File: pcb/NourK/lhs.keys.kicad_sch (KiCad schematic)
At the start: 33 parts, among them SW10 OSKEY, SW11 GRAVE, SW12 A, SW13 S, SW14 D, SW15 F, SW16 G, SW17 LEFT_SHIFT, SW18 Z, SW19 X, SW20 C, SW21 V, SW22 B, SW23 LEFT_CTRL, SW24 LAYER1, SW25 LAYER2, SW26 LEFT_ALT, SW27 SPACE, SW3 ESCAPE, SW4 TAB, SW5 Q, SW6 W, SW7 E, SW8 R, SW9 T

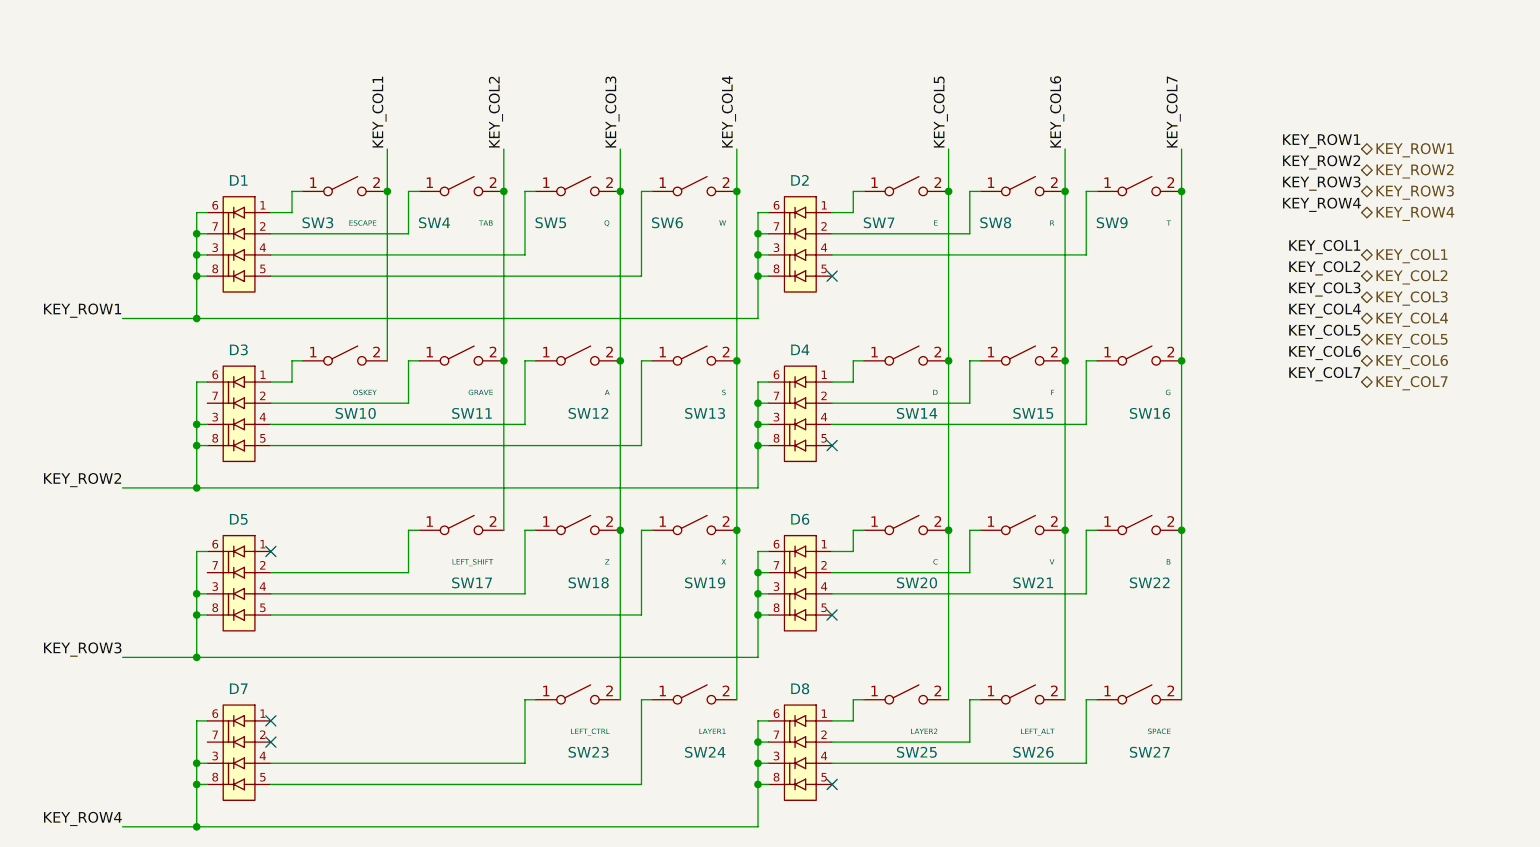
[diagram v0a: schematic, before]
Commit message: Add RHS schematics sheets
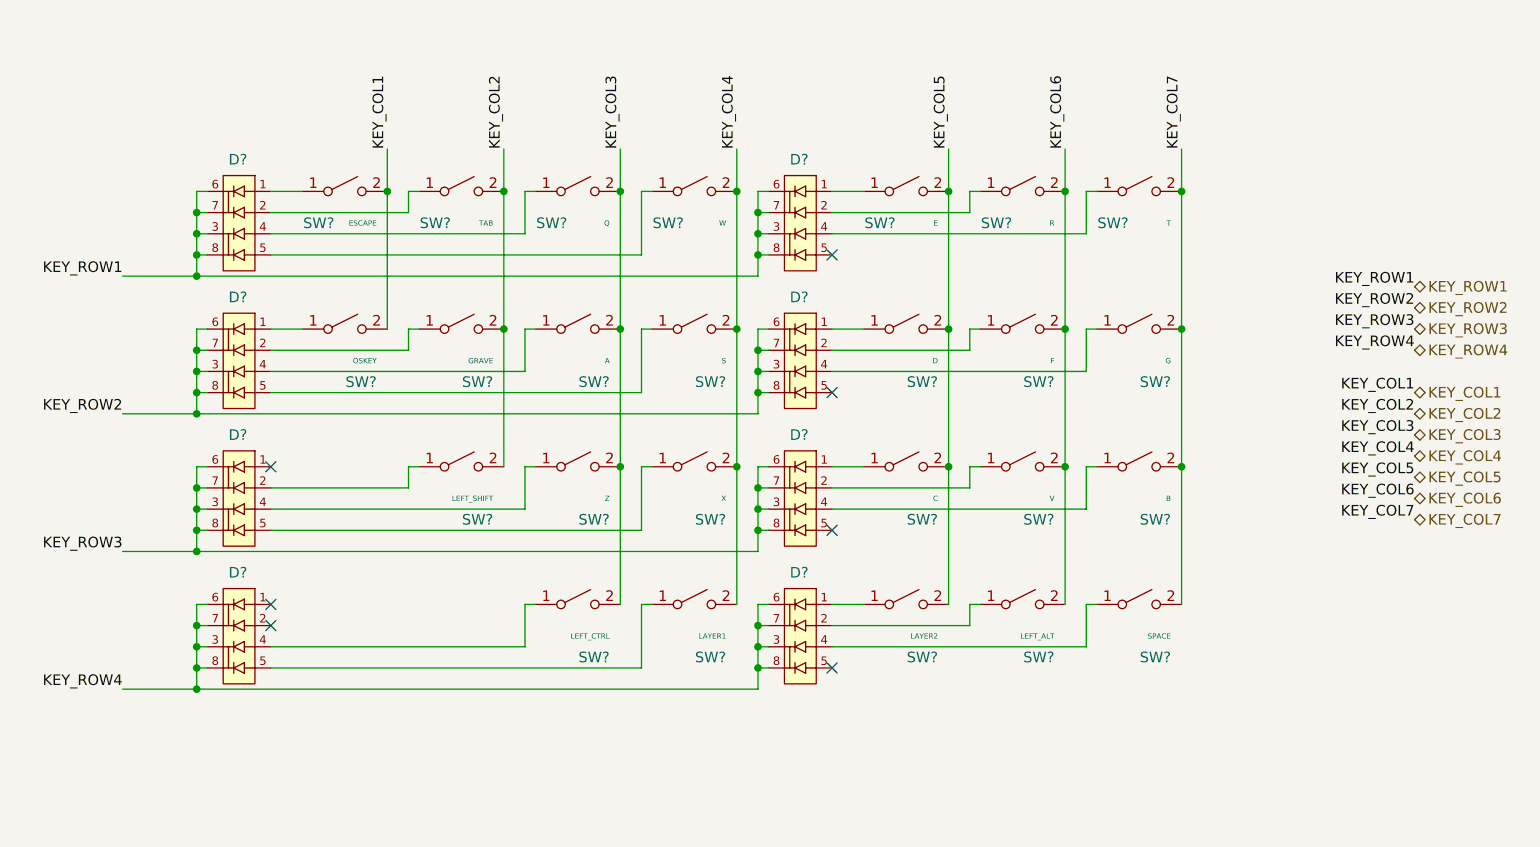
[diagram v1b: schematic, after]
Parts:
- removed D1, D2, D3, D4, D5, D6, D7, D8: BAV70SRAZ, Nour_KB:DIO_BAV70SRAZ, symbol Nour_KB:BAV70SRAZ
- removed SW10: OSKEY, Keebio-Parts:MX-Alps-Choc-1U-NoLED, symbol Switch:SW_SPST
- removed SW11: GRAVE, Keebio-Parts:MX-Alps-Choc-1U-NoLED, symbol Switch:SW_SPST
- removed SW12: A, Keebio-Parts:MX-Alps-Choc-1U-NoLED, symbol Switch:SW_SPST
- removed SW13: S, Keebio-Parts:MX-Alps-Choc-1U-NoLED, symbol Switch:SW_SPST
- removed SW14: D, Keebio-Parts:MX-Alps-Choc-1U-NoLED, symbol Switch:SW_SPST
- removed SW15: F, Keebio-Parts:MX-Alps-Choc-1U-NoLED, symbol Switch:SW_SPST
- removed SW16: G, Keebio-Parts:MX-Alps-Choc-1U-NoLED, symbol Switch:SW_SPST
- removed SW17: LEFT_SHIFT, Keebio-Parts:MX-Alps-Choc-1U-NoLED, symbol Switch:SW_SPST
- removed SW18: Z, Keebio-Parts:MX-Alps-Choc-1U-NoLED, symbol Switch:SW_SPST
- removed SW19: X, Keebio-Parts:MX-Alps-Choc-1U-NoLED, symbol Switch:SW_SPST
- removed SW20: C, Keebio-Parts:MX-Alps-Choc-1U-NoLED, symbol Switch:SW_SPST
- removed SW21: V, Keebio-Parts:MX-Alps-Choc-1U-NoLED, symbol Switch:SW_SPST
- removed SW22: B, Keebio-Parts:MX-Alps-Choc-1U-NoLED, symbol Switch:SW_SPST
- removed SW23: LEFT_CTRL, Keebio-Parts:MX-Alps-Choc-1U-NoLED, symbol Switch:SW_SPST
- removed SW24: LAYER1, Keebio-Parts:MX-Alps-Choc-1U-NoLED, symbol Switch:SW_SPST
- removed SW25: LAYER2, Keebio-Parts:MX-Alps-Choc-1U-NoLED, symbol Switch:SW_SPST
- removed SW26: LEFT_ALT, Keebio-Parts:MX-Alps-Choc-1U-NoLED, symbol Switch:SW_SPST
- removed SW27: SPACE, Keebio-Parts:MX-Alps-Choc-1U-NoLED, symbol Switch:SW_SPST
- removed SW3: ESCAPE, Keebio-Parts:MX-Alps-Choc-1U-NoLED, symbol Switch:SW_SPST
- removed SW4: TAB, Keebio-Parts:MX-Alps-Choc-1U-NoLED, symbol Switch:SW_SPST
- removed SW5: Q, Keebio-Parts:MX-Alps-Choc-1U-NoLED, symbol Switch:SW_SPST
- removed SW6: W, Keebio-Parts:MX-Alps-Choc-1U-NoLED, symbol Switch:SW_SPST
- removed SW7: E, Keebio-Parts:MX-Alps-Choc-1U-NoLED, symbol Switch:SW_SPST
- removed SW8: R, Keebio-Parts:MX-Alps-Choc-1U-NoLED, symbol Switch:SW_SPST
- removed SW9: T, Keebio-Parts:MX-Alps-Choc-1U-NoLED, symbol Switch:SW_SPST
- added D? (x8): BAV70SRAZ, Nour_KB:DIO_BAV70SRAZ, symbol Nour_KB:BAV70SRAZ
- added SW?: B, Keebio-Parts:MX-Alps-Choc-1U-NoLED, symbol Switch:SW_SPST
- added SW?: OSKEY, Keebio-Parts:MX-Alps-Choc-1U-NoLED, symbol Switch:SW_SPST
- added SW?: G, Keebio-Parts:MX-Alps-Choc-1U-NoLED, symbol Switch:SW_SPST
- added SW?: T, Keebio-Parts:MX-Alps-Choc-1U-NoLED, symbol Switch:SW_SPST
- added SW?: C, Keebio-Parts:MX-Alps-Choc-1U-NoLED, symbol Switch:SW_SPST
- added SW?: S, Keebio-Parts:MX-Alps-Choc-1U-NoLED, symbol Switch:SW_SPST
- added SW?: ESCAPE, Keebio-Parts:MX-Alps-Choc-1U-NoLED, symbol Switch:SW_SPST
- added SW?: Z, Keebio-Parts:MX-Alps-Choc-1U-NoLED, symbol Switch:SW_SPST
- added SW?: W, Keebio-Parts:MX-Alps-Choc-1U-NoLED, symbol Switch:SW_SPST
- added SW?: LAYER1, Keebio-Parts:MX-Alps-Choc-1U-NoLED, symbol Switch:SW_SPST
- added SW?: SPACE, Keebio-Parts:MX-Alps-Choc-1U-NoLED, symbol Switch:SW_SPST
- added SW?: R, Keebio-Parts:MX-Alps-Choc-1U-NoLED, symbol Switch:SW_SPST
- added SW?: LEFT_ALT, Keebio-Parts:MX-Alps-Choc-1U-NoLED, symbol Switch:SW_SPST
- added SW?: Q, Keebio-Parts:MX-Alps-Choc-1U-NoLED, symbol Switch:SW_SPST
- added SW?: V, Keebio-Parts:MX-Alps-Choc-1U-NoLED, symbol Switch:SW_SPST
- added SW?: TAB, Keebio-Parts:MX-Alps-Choc-1U-NoLED, symbol Switch:SW_SPST
- added SW?: LEFT_CTRL, Keebio-Parts:MX-Alps-Choc-1U-NoLED, symbol Switch:SW_SPST
- added SW?: D, Keebio-Parts:MX-Alps-Choc-1U-NoLED, symbol Switch:SW_SPST
- added SW?: F, Keebio-Parts:MX-Alps-Choc-1U-NoLED, symbol Switch:SW_SPST
- added SW?: GRAVE, Keebio-Parts:MX-Alps-Choc-1U-NoLED, symbol Switch:SW_SPST
- added SW?: LEFT_SHIFT, Keebio-Parts:MX-Alps-Choc-1U-NoLED, symbol Switch:SW_SPST
- added SW?: LAYER2, Keebio-Parts:MX-Alps-Choc-1U-NoLED, symbol Switch:SW_SPST
- added SW?: E, Keebio-Parts:MX-Alps-Choc-1U-NoLED, symbol Switch:SW_SPST
- added SW?: A, Keebio-Parts:MX-Alps-Choc-1U-NoLED, symbol Switch:SW_SPST
- added SW?: X, Keebio-Parts:MX-Alps-Choc-1U-NoLED, symbol Switch:SW_SPST
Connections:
- net KEY_COL1: now also SW?.2 (B), SW?.2 (B)
- net KEY_COL2: now also SW?.2 (B), SW?.2 (B), SW?.2 (B)
- net KEY_COL3: now also SW?.2 (B), SW?.2 (B), SW?.2 (B), SW?.2 (B)
- net KEY_COL4: now also SW?.2 (B), SW?.2 (B), SW?.2 (B), SW?.2 (B)
- net KEY_COL5: now also SW?.2 (B), SW?.2 (B), SW?.2 (B), SW?.2 (B)
- net KEY_COL6: now also SW?.2 (B), SW?.2 (B), SW?.2 (B), SW?.2 (B)
- net KEY_COL7: now also SW?.2 (B), SW?.2 (B), SW?.2 (B), SW?.2 (B)
- net KEY_ROW1: now also D?.3, D?.3, D?.6, D?.6, D?.7, D?.7, D?.8, D?.8
- net KEY_ROW2: now also D?.3, D?.3, D?.6, D?.6, D?.7, D?.7, D?.8, D?.8
- net KEY_ROW3: now also D?.3, D?.3, D?.6, D?.6, D?.7, D?.7, D?.8, D?.8
- net KEY_ROW4: now also D?.3, D?.3, D?.6, D?.6, D?.7, D?.7, D?.8, D?.8
- new net: D?.4, SW?.1 (A) (x8)
- new net: D?.1, SW?.1 (A) (x6)
- new net: D?.5, SW?.1 (A) (x4)
- new net: D?.2, SW?.1 (A) (x7)

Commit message: Draft LHS tracks
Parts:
- gave numbers to parts that had none: 33
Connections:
- net at SW53.1 (A): now also D48.1; no longer D48.4
- net at SW31.1 (A): now also D43.5; no longer D43.1
- net at SW52.1 (A): now also D47.1; no longer D47.4
- net at SW51.1 (A): now also D46.1; no longer D46.4
- net at SW45.1 (A): now also D48.5; no longer D48.1
- net at D45.1: now also SW42.1 (A)
- net at D45.2: now also SW38.1 (A)
- net at D45.4: no longer SW38.1 (A)
- net at D45.5: no longer SW42.1 (A)
- net at SW40.1 (A): now also D43.1; no longer D43.5
- net at SW30.1 (A): now also D42.5; no longer D42.1
- net at SW37.1 (A): now also D44.2; no longer D44.4
- net at SW39.1 (A): now also D42.1; no longer D42.5
- net at SW44.1 (A): now also D47.5; no longer D47.1
- net at SW54.1 (A): now also D49.1; no longer D49.4
- net at SW35.1 (A): now also D42.2; no longer D42.4
- net at SW32.1 (A): now also D42.4; no longer D42.2
- net at SW43.1 (A): now also D46.5; no longer D46.1
- net at SW33.1 (A): now also D43.4; no longer D43.2
- net at SW34.1 (A): now also D44.4; no longer D44.2
- net at SW36.1 (A): now also D43.2; no longer D43.4
- net at SW46.1 (A): now also D49.5; no longer D49.1
- net at D44.1: now also SW41.1 (A)
- net at D44.5: no longer SW41.1 (A)
- net KEY_COL1 renamed KEY.COL1
- net KEY_COL2 renamed KEY.COL2
- net KEY_COL3 renamed KEY.COL3
- net KEY_COL4 renamed KEY.COL4
- net KEY_COL5 renamed KEY.COL5
- net KEY_COL6 renamed KEY.COL6
- net KEY_COL7 renamed KEY.COL7
- net KEY_ROW1 renamed KEY.ROW1
- net KEY_ROW2 renamed KEY.ROW2
- net KEY_ROW3 renamed KEY.ROW3
- net KEY_ROW4 renamed KEY.ROW4
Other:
- moved on the sheet: D42, D43, D44, D45, D46, D47, D48, D49

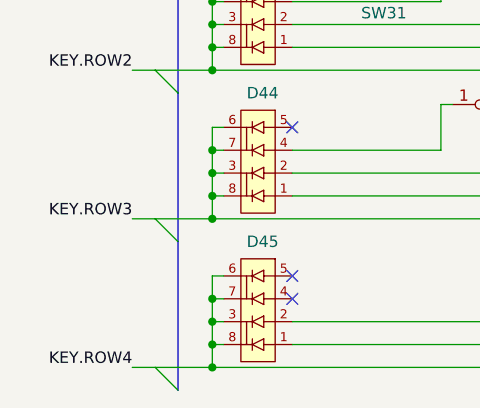
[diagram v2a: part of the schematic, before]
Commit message: RHS and LHS wire complete and initial DRC
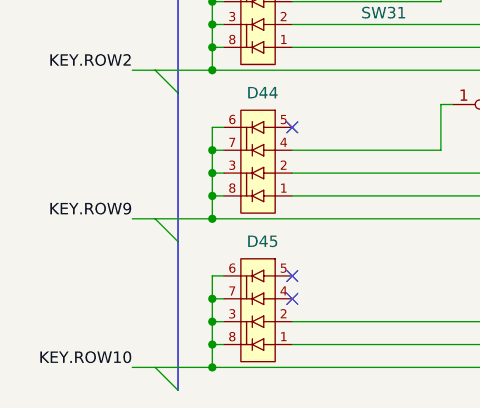
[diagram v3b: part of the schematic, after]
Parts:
- SW30, SW31, SW32, SW33, SW34, SW35, SW36, SW37, SW38, SW39, SW40, SW41, SW42, SW43, SW44, SW45, SW46, SW47, SW48, SW49, SW50, SW51, SW52, SW53, SW54: footprint Keebio-Parts:MX-Alps-Choc-1U-NoLED -> Nour_KB:MX_Choc_1U
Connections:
- net KEY.ROW3 renamed KEY.ROW9
- net KEY.ROW4 renamed KEY.ROW10
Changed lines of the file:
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@@
     (effects (font (size 1.27 1.27)) (justify right bottom))
   )
-  (label "KEY.ROW3" (at 69.85 114.3 180)
+  (label "KEY.ROW9" (at 69.85 114.3 180)
     (effects (font (size 1.27 1.27)) (justify right bottom))
   )
-  (label "KEY.ROW4" (at 69.85 130.81 180)
+  (label "KEY.ROW10" (at 69.85 130.81 180)
     (effects (font (size 1.27 1.27)) (justify right bottom))
   )
@@
       (effects (font (size 0.63 0.63)) (justify right))
     )
-    (property "Footprint" "Keebio-Parts:MX-Alps-Choc-1U-NoLED" (id 2) (at 191.77 101.6 0)
+    (property "Footprint" "Nour_KB:MX_Choc_1U" (id 2) (at 191.77 101.6 0)
       (effects (font (size 1.27 1.27)) hide)
     )
@@
       (effects (font (size 0.63 0.63)) (justify right))
     )
-    (property "Footprint" "Keebio-Parts:MX-Alps-Choc-1U-NoLED" (id 2) (at 96.52 85.09 0)
+    (property "Footprint" "Nour_KB:MX_Choc_1U" (id 2) (at 96.52 85.09 0)
       (effects (font (size 1.27 1.27)) hide)
     )
@@
       (effects (font (size 0.63 0.63)) (justify right))
     )
-    (property "Footprint" "Keebio-Parts:MX-Alps-Choc-1U-NoLED" (id 2) (at 191.77 85.09 0)
+    (property "Footprint" "Nour_KB:MX_Choc_1U" (id 2) (at 191.77 85.09 0)
       (effects (font (size 1.27 1.27)) hide)
     )
@@
       (effects (font (size 0.63 0.63)) (justify right))
     )
-    (property "Footprint" "Keebio-Parts:MX-Alps-Choc-1U-NoLED" (id 2) (at 191.77 68.58 0)
+    (property "Footprint" "Nour_KB:MX_Choc_1U" (id 2) (at 191.77 68.58 0)
       (effects (font (size 1.27 1.27)) hide)
     )
@@
       (effects (font (size 0.63 0.63)) (justify right))
     )
-    (property "Footprint" "Keebio-Parts:MX-Alps-Choc-1U-NoLED" (id 2) (at 163.83 101.6 0)
+    (property "Footprint" "Nour_KB:MX_Choc_1U" (id 2) (at 163.83 101.6 0)
       (effects (font (size 1.27 1.27)) hide)
     )
@@
       (effects (font (size 0.63 0.63)) (justify right))
     )
-    (property "Footprint" "Keebio-Parts:MX-Alps-Choc-1U-NoLED" (id 2) (at 138.43 85.09 0)
+    (property "Footprint" "Nour_KB:MX_Choc_1U" (id 2) (at 138.43 85.09 0)
       (effects (font (size 1.27 1.27)) hide)
     )
@@
       (effects (font (size 0.63 0.63)) (justify right))
     )
-    (property "Footprint" "Keebio-Parts:MX-Alps-Choc-1U-NoLED" (id 2) (at 96.52 68.58 0)
+    (property "Footprint" "Nour_KB:MX_Choc_1U" (id 2) (at 96.52 68.58 0)
       (effects (font (size 1.27 1.27)) hide)
     )
@@
       (effects (font (size 0.63 0.63)) (justify right))
     )
-    (property "Footprint" "Keebio-Parts:MX-Alps-Choc-1U-NoLED" (id 2) (at 124.46 101.6 0)
+    (property "Footprint" "Nour_KB:MX_Choc_1U" (id 2) (at 124.46 101.6 0)
       (effects (font (size 1.27 1.27)) hide)
     )
@@
       (effects (font (size 0.63 0.63)) (justify right))
     )
-    (property "Footprint" "Keebio-Parts:MX-Alps-Choc-1U-NoLED" (id 2) (at 138.43 68.58 0)
+    (property "Footprint" "Nour_KB:MX_Choc_1U" (id 2) (at 138.43 68.58 0)
       (effects (font (size 1.27 1.27)) hide)
     )
@@
       (effects (font (size 0.63 0.63)) (justify right))
     )
-    (property "Footprint" "Keebio-Parts:MX-Alps-Choc-1U-NoLED" (id 2) (at 138.43 118.11 0)
+    (property "Footprint" "Nour_KB:MX_Choc_1U" (id 2) (at 138.43 118.11 0)
       (effects (font (size 1.27 1.27)) hide)
     )
@@
       (effects (font (size 0.63 0.63)) (justify right))
     )
-    (property "Footprint" "Keebio-Parts:MX-Alps-Choc-1U-NoLED" (id 2) (at 191.77 118.11 0)
+    (property "Footprint" "Nour_KB:MX_Choc_1U" (id 2) (at 191.77 118.11 0)
       (effects (font (size 1.27 1.27)) hide)
     )
@@
       (effects (font (size 0.63 0.63)) (justify right))
     )
-    (property "Footprint" "Keebio-Parts:MX-Alps-Choc-1U-NoLED" (id 2) (at 177.8 68.58 0)
+    (property "Footprint" "Nour_KB:MX_Choc_1U" (id 2) (at 177.8 68.58 0)
       (effects (font (size 1.27 1.27)) hide)
     )
@@
       (effects (font (size 0.63 0.63)) (justify right))
     )
-    (property "Footprint" "Keebio-Parts:MX-Alps-Choc-1U-NoLED" (id 2) (at 177.8 118.11 0)
+    (property "Footprint" "Nour_KB:MX_Choc_1U" (id 2) (at 177.8 118.11 0)
       (effects (font (size 1.27 1.27)) hide)
     )
@@
       (effects (font (size 0.63 0.63)) (justify right))
     )
-    (property "Footprint" "Keebio-Parts:MX-Alps-Choc-1U-NoLED" (id 2) (at 124.46 68.58 0)
+    (property "Footprint" "Nour_KB:MX_Choc_1U" (id 2) (at 124.46 68.58 0)
       (effects (font (size 1.27 1.27)) hide)
     )
@@
       (effects (font (size 0.63 0.63)) (justify right))
     )
-    (property "Footprint" "Keebio-Parts:MX-Alps-Choc-1U-NoLED" (id 2) (at 177.8 101.6 0)
+    (property "Footprint" "Nour_KB:MX_Choc_1U" (id 2) (at 177.8 101.6 0)
       (effects (font (size 1.27 1.27)) hide)
     )
@@
       (effects (font (size 0.63 0.63)) (justify right))
     )
-    (property "Footprint" "Keebio-Parts:MX-Alps-Choc-1U-NoLED" (id 2) (at 110.49 68.58 0)
+    (property "Footprint" "Nour_KB:MX_Choc_1U" (id 2) (at 110.49 68.58 0)
       (effects (font (size 1.27 1.27)) hide)
     )
@@
       (effects (font (size 0.63 0.63)) (justify right))
     )
-    (property "Footprint" "Keebio-Parts:MX-Alps-Choc-1U-NoLED" (id 2) (at 124.46 118.11 0)
+    (property "Footprint" "Nour_KB:MX_Choc_1U" (id 2) (at 124.46 118.11 0)
       (effects (font (size 1.27 1.27)) hide)
     )
@@
       (effects (font (size 0.63 0.63)) (justify right))
     )
-    (property "Footprint" "Keebio-Parts:MX-Alps-Choc-1U-NoLED" (id 2) (at 163.83 85.09 0)
+    (property "Footprint" "Nour_KB:MX_Choc_1U" (id 2) (at 163.83 85.09 0)
       (effects (font (size 1.27 1.27)) hide)
     )
@@
       (effects (font (size 0.63 0.63)) (justify right))
     )
-    (property "Footprint" "Keebio-Parts:MX-Alps-Choc-1U-NoLED" (id 2) (at 177.8 85.09 0)
+    (property "Footprint" "Nour_KB:MX_Choc_1U" (id 2) (at 177.8 85.09 0)
       (effects (font (size 1.27 1.27)) hide)
     )
@@
       (effects (font (size 0.63 0.63)) (justify right))
     )
-    (property "Footprint" "Keebio-Parts:MX-Alps-Choc-1U-NoLED" (id 2) (at 110.49 85.09 0)
+    (property "Footprint" "Nour_KB:MX_Choc_1U" (id 2) (at 110.49 85.09 0)
       (effects (font (size 1.27 1.27)) hide)
     )
@@
       (effects (font (size 0.63 0.63)) (justify right))
     )
-    (property "Footprint" "Keebio-Parts:MX-Alps-Choc-1U-NoLED" (id 2) (at 110.49 101.6 0)
+    (property "Footprint" "Nour_KB:MX_Choc_1U" (id 2) (at 110.49 101.6 0)
       (effects (font (size 1.27 1.27)) hide)
     )
@@
       (effects (font (size 0.63 0.63)) (justify right))
     )
-    (property "Footprint" "Keebio-Parts:MX-Alps-Choc-1U-NoLED" (id 2) (at 163.83 118.11 0)
+    (property "Footprint" "Nour_KB:MX_Choc_1U" (id 2) (at 163.83 118.11 0)
       (effects (font (size 1.27 1.27)) hide)
     )
@@
       (effects (font (size 0.63 0.63)) (justify right))
     )
-    (property "Footprint" "Keebio-Parts:MX-Alps-Choc-1U-NoLED" (id 2) (at 163.83 68.58 0)
+    (property "Footprint" "Nour_KB:MX_Choc_1U" (id 2) (at 163.83 68.58 0)
       (effects (font (size 1.27 1.27)) hide)
     )
@@
       (effects (font (size 0.63 0.63)) (justify right))
     )
-    (property "Footprint" "Keebio-Parts:MX-Alps-Choc-1U-NoLED" (id 2) (at 124.46 85.09 0)
+    (property "Footprint" "Nour_KB:MX_Choc_1U" (id 2) (at 124.46 85.09 0)
       (effects (font (size 1.27 1.27)) hide)
     )
@@
       (effects (font (size 0.63 0.63)) (justify right))
     )
-    (property "Footprint" "Keebio-Parts:MX-Alps-Choc-1U-NoLED" (id 2) (at 138.43 101.6 0)
-      (effects (font (size 1.27 1.27)) hide)
-    )
+    (property "Footprint" "Nour_KB:MX_Choc_1U" (id 2) (at 138.43 101.6 0)
+      (effects (font (size 1.27 1.27)) hide)
+    )
